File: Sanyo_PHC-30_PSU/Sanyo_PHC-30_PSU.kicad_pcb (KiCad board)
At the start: 2 copper layers, 82 x 71 mm, 17 parts, among them J1 To Data Recorder, J2 12VDC In, J3 To Motherboard, J4 Ground Strap, U1 PSU2-5, U2 NKE1212SC

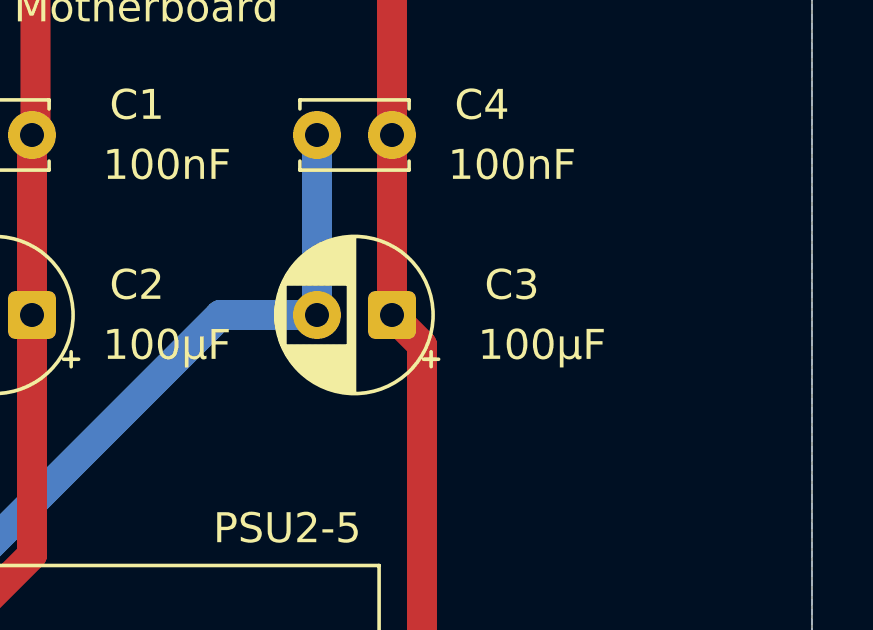
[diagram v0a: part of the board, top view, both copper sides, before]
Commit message: Fixed C3 orientation
+ve leg of electrolytic should be connected to GND and -ve leg to -12V ... GND is more positive than -12V, duh
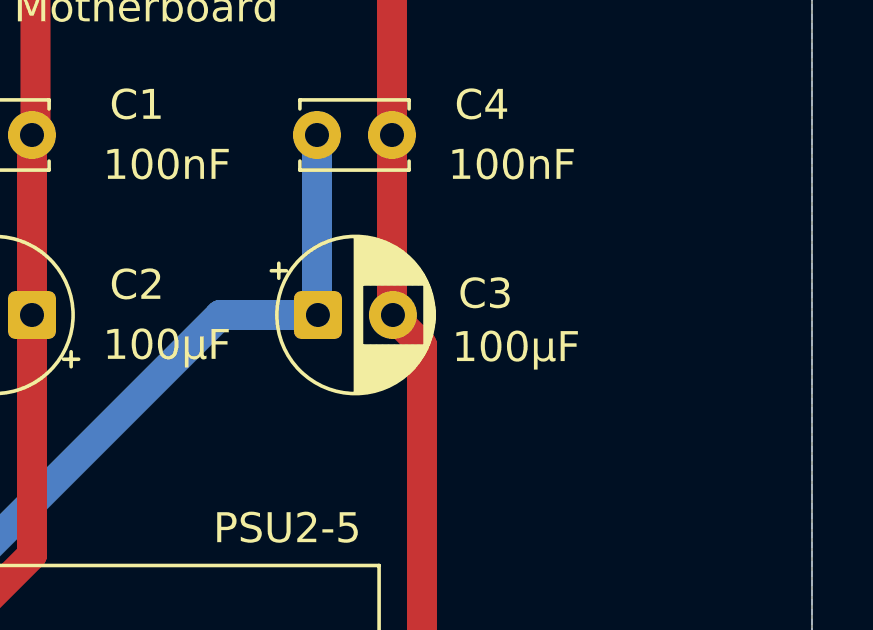
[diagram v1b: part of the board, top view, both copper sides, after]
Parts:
- moved C3 2.47 mm to (157.3, 77.5), turned to 0 degrees
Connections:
- C3 pad 1: /-12V -> /GND
- C3 pad 2: /GND -> /-12V
